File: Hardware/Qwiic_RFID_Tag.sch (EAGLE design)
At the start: 29 parts, among them J1 Qwiic, J2 Qwiic, U1 ST25DV64KC

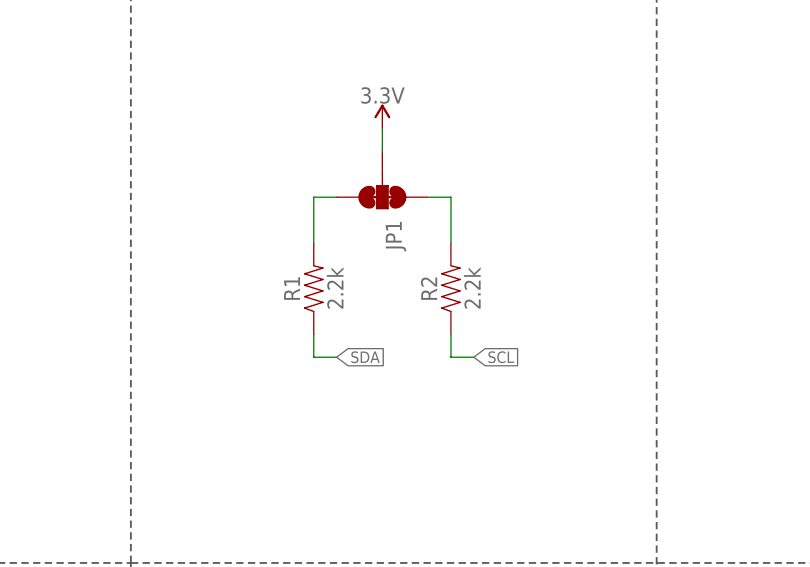
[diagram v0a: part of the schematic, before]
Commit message: Fixed misaligned mounting hole; trimmed long schematic segment.
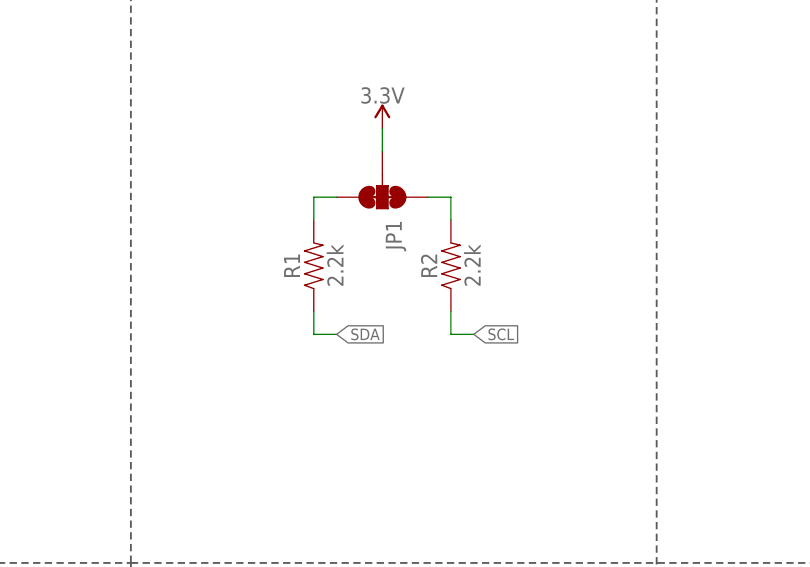
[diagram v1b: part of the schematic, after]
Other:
- moved on the sheet: R1, R2
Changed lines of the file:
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@@
 <attribute name="VALUE" x="174.625" y="122.428" size="1.778" layer="96" font="vector" rot="R90" align="top-left"/>
 </instance>
-<instance part="R1" gate="G$1" x="109.22" y="134.62" smashed="yes" rot="R90">
-<attribute name="NAME" x="107.696" y="134.62" size="1.778" layer="95" font="vector" rot="R90" align="bottom-center"/>
-<attribute name="VALUE" x="110.744" y="134.62" size="1.778" layer="96" font="vector" rot="R90" align="top-center"/>
-</instance>
-<instance part="R2" gate="G$1" x="124.46" y="134.62" smashed="yes" rot="R90">
-<attribute name="NAME" x="122.936" y="134.62" size="1.778" layer="95" font="vector" rot="R90" align="bottom-center"/>
-<attribute name="VALUE" x="125.984" y="134.62" size="1.778" layer="96" font="vector" rot="R90" align="top-center"/>
+<instance part="R1" gate="G$1" x="109.22" y="137.16" smashed="yes" rot="R90">
+<attribute name="NAME" x="107.696" y="137.16" size="1.778" layer="95" font="vector" rot="R90" align="bottom-center"/>
+<attribute name="VALUE" x="110.744" y="137.16" size="1.778" layer="96" font="vector" rot="R90" align="top-center"/>
+</instance>
+<instance part="R2" gate="G$1" x="124.46" y="137.16" smashed="yes" rot="R90">
+<attribute name="NAME" x="122.936" y="137.16" size="1.778" layer="95" font="vector" rot="R90" align="bottom-center"/>
+<attribute name="VALUE" x="125.984" y="137.16" size="1.778" layer="96" font="vector" rot="R90" align="top-center"/>
 </instance>
 <instance part="JP1" gate="G$1" x="116.84" y="144.78" smashed="yes" rot="R270">
@@
 <segment>
 <pinref part="R2" gate="G$1" pin="1"/>
-<wire x1="124.46" y1="129.54" x2="124.46" y2="127" width="0.1524" layer="91"/>
-<wire x1="124.46" y1="127" x2="127" y2="127" width="0.1524" layer="91"/>
-<label x="127" y="127" size="1.27" layer="95" xref="yes"/>
+<wire x1="124.46" y1="132.08" x2="124.46" y2="129.54" width="0.1524" layer="91"/>
+<wire x1="124.46" y1="129.54" x2="127" y2="129.54" width="0.1524" layer="91"/>
+<label x="127" y="129.54" size="1.27" layer="95" xref="yes"/>
 </segment>
 <segment>
@@
 <segment>
 <pinref part="R1" gate="G$1" pin="1"/>
-<wire x1="109.22" y1="129.54" x2="109.22" y2="127" width="0.1524" layer="91"/>
-<wire x1="109.22" y1="127" x2="111.76" y2="127" width="0.1524" layer="91"/>
-<label x="111.76" y="127" size="1.27" layer="95" xref="yes"/>
+<wire x1="109.22" y1="132.08" x2="109.22" y2="129.54" width="0.1524" layer="91"/>
+<wire x1="109.22" y1="129.54" x2="111.76" y2="129.54" width="0.1524" layer="91"/>
+<label x="111.76" y="129.54" size="1.27" layer="95" xref="yes"/>
 </segment>
 <segment>
@@
 <segment>
 <pinref part="R1" gate="G$1" pin="2"/>
-<wire x1="109.22" y1="139.7" x2="109.22" y2="144.78" width="0.1524" layer="91"/>
+<wire x1="109.22" y1="142.24" x2="109.22" y2="144.78" width="0.1524" layer="91"/>
 <wire x1="109.22" y1="144.78" x2="111.76" y2="144.78" width="0.1524" layer="91"/>
 <pinref part="JP1" gate="G$1" pin="3"/>
@@
 <pinref part="R2" gate="G$1" pin="2"/>
 <wire x1="121.92" y1="144.78" x2="124.46" y2="144.78" width="0.1524" layer="91"/>
-<wire x1="124.46" y1="144.78" x2="124.46" y2="139.7" width="0.1524" layer="91"/>
+<wire x1="124.46" y1="144.78" x2="124.46" y2="142.24" width="0.1524" layer="91"/>
 <pinref part="JP1" gate="G$1" pin="1"/>
 </segment>

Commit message: Created PCB production files.
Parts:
- LOGO2, LOGO3: value QWIIC_LOGO_4MM -> QWIIC_LOGO_7MM; device SparkFun-Aesthetics:QWIIC_LOGO_4MM -> SparkFun-Aesthetics:QWIIC_LOGO_7MM
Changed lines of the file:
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@@
 <part name="FD4" library="SparkFun-Aesthetics" deviceset="FIDUCIAL" device="1X2"/>
 <part name="LOGO1" library="SparkFun-Aesthetics" deviceset="OSHW-LOGO" device="MINI" value="OSHW-LOGOMINI"/>
-<part name="LOGO2" library="SparkFun-Aesthetics" deviceset="QWIIC_LOGO" device="_4MM" value="QWIIC_LOGO_4MM"/>
-<part name="LOGO3" library="SparkFun-Aesthetics" deviceset="QWIIC_LOGO" device="_4MM" value="QWIIC_LOGO_4MM"/>
+<part name="LOGO3" library="SparkFun-Aesthetics" deviceset="QWIIC_LOGO" device="_7MM" value="QWIIC_LOGO_7MM"/>
 <part name="H1" library="SparkFun-Hardware" deviceset="STAND-OFF" device=""/>
 <part name="H2" library="SparkFun-Hardware" deviceset="STAND-OFF" device=""/>
@@
 <part name="U$1" library="SparkX" deviceset="SPARKX-LOGO" device="5"/>
 <part name="U$2" library="SparkX" deviceset="SPARKX-LOGO" device="5"/>
+<part name="LOGO2" library="SparkFun-Aesthetics" deviceset="QWIIC_LOGO" device="_7MM" value="QWIIC_LOGO_7MM"/>
 </parts>
 <sheets>
@@
 <instance part="FD4" gate="G$1" x="233.68" y="30.48" smashed="yes"/>
 <instance part="LOGO1" gate="G$1" x="83.82" y="25.4" smashed="yes"/>
-<instance part="LOGO2" gate="G$1" x="116.84" y="17.78" smashed="yes"/>
-<instance part="LOGO3" gate="G$1" x="116.84" y="17.78" smashed="yes"/>
+<instance part="LOGO3" gate="G$1" x="116.84" y="20.32" smashed="yes"/>
 <instance part="H1" gate="G$1" x="238.76" y="27.94" smashed="yes"/>
 <instance part="H2" gate="G$1" x="241.3" y="27.94" smashed="yes"/>
@@
 <instance part="U$1" gate="G$1" x="116.84" y="27.94" smashed="yes"/>
 <instance part="U$2" gate="G$1" x="116.84" y="27.94" smashed="yes"/>
+<instance part="LOGO2" gate="G$1" x="116.84" y="20.32" smashed="yes"/>
 </instances>
 <busses>

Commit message: X02 PCB
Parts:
- removed LOGO2: QWIIC_LOGO_7MM, SparkFun-Aesthetics:QWIIC_LOGO_7MM
- FRAME1: REV (none) -> X02; VERSION (none) -> x01
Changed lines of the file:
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@@
 <setting verticaltext="up"/>
 </settings>
-<grid distance="0.1" unitdist="inch" unit="inch" style="lines" multiple="1" display="no" altdistance="0.01" altunitdist="inch" altunit="inch"/>
+<grid distance="0.1" unitdist="inch" unit="inch" style="lines" multiple="1" display="no" altdistance="0.05" altunitdist="inch" altunit="inch"/>
 <layers>
 <layer number="1" name="Top" color="4" fill="1" visible="no" active="no"/>
 <layer number="2" name="Route2" color="1" fill="3" visible="no" active="no"/>
+<layer number="3" name="Route3" color="4" fill="3" visible="no" active="no"/>
+<layer number="4" name="Route4" color="1" fill="4" visible="no" active="no"/>
+<layer number="5" name="Route5" color="4" fill="4" visible="no" active="no"/>
+<layer number="6" name="Route6" color="1" fill="8" visible="no" active="no"/>
+<layer number="7" name="Route7" color="4" fill="8" visible="no" active="no"/>
+<layer number="8" name="Route8" color="1" fill="2" visible="no" active="no"/>
+<layer number="9" name="Route9" color="4" fill="2" visible="no" active="no"/>
+<layer number="10" name="Route10" color="1" fill="7" visible="no" active="no"/>
+<layer number="11" name="Route11" color="4" fill="7" visible="no" active="no"/>
+<layer number="12" name="Route12" color="1" fill="5" visible="no" active="no"/>
+<layer number="13" name="Route13" color="4" fill="5" visible="no" active="no"/>
+<layer number="14" name="Route14" color="1" fill="6" visible="no" active="no"/>
 <layer number="15" name="Route15" color="4" fill="6" visible="no" active="no"/>
 <layer number="16" name="Bottom" color="1" fill="1" visible="no" active="no"/>
@@
 <part name="FRAME1" library="SparkFun-Aesthetics" deviceset="FRAME-LETTER" device="NO_PACKAGE">
 <attribute name="DESIGNER" value="Ricardo Ramos"/>
+<attribute name="REV" value="X02"/>
+<attribute name="VERSION" value="x01"/>
 </part>
 <part name="L1" library="SparkFun-Coils" deviceset="PCB_4UH_INDUCTOR" device=""/>
@@
 <part name="U$1" library="SparkX" deviceset="SPARKX-LOGO" device="5"/>
 <part name="U$2" library="SparkX" deviceset="SPARKX-LOGO" device="5"/>
-<part name="LOGO2" library="SparkFun-Aesthetics" deviceset="QWIIC_LOGO" device="_7MM" value="QWIIC_LOGO_7MM"/>
 </parts>
 <sheets>
 <sheet>
 <plain>
-<text x="200.66" y="93.98" size="2.54" layer="94" align="center">Qwiic Connectors</text>
-<text x="162.56" y="168.91" size="1.27" layer="97">Cut trace to disable LED</text>
-<text x="210.82" y="168.91" size="1.27" layer="97">Cut trace to remove !GPO! pullup</text>
-<text x="119.38" y="93.98" size="2.54" layer="94" align="center">0.1" Header</text>
-<text x="45.72" y="93.98" size="2.54" layer="94" align="center">PCB antenna</text>
-<text x="116.84" y="172.72" size="2.54" layer="94" align="center">I2C Pullup</text>
-<text x="172.72" y="172.72" size="2.54" layer="94" align="center">Power LED</text>
-<text x="223.52" y="172.72" size="2.54" layer="94" align="center">!GPO! Pullup</text>
-<text x="45.72" y="170.18" size="2.54" layer="94" align="center">ST25DV64KC Dynamic RFID Tag</text>
-<text x="27.94" y="40.64" size="2.54" layer="94" align="center">Power decoupling</text>
+<text x="200.66" y="93.98" size="2.54" layer="94" font="vector" align="center">Qwiic Connectors</text>
+<text x="162.56" y="168.91" size="1.27" layer="97" font="vector">Cut trace to disable LED</text>
+<text x="210.82" y="168.91" size="1.27" layer="97" font="vector">Cut trace to remove !GPO! pullup</text>
+<text x="119.38" y="93.98" size="2.54" layer="94" font="vector" align="center">0.1" Header</text>
+<text x="45.72" y="93.98" size="2.54" layer="94" font="vector" align="center">PCB antenna</text>
+<text x="116.84" y="172.72" size="2.54" layer="94" font="vector" align="center">I2C Pullup</text>
+<text x="172.72" y="172.72" size="2.54" layer="94" font="vector" align="center">Power LED</text>
+<text x="223.52" y="172.72" size="2.54" layer="94" font="vector" align="center">!GPO! Pullup</text>
+<text x="45.72" y="170.18" size="2.54" layer="94" font="vector" align="center">ST25DV64KC Dynamic RFID Tag</text>
+<text x="27.94" y="40.64" size="2.54" layer="94" font="vector" align="center">Power decoupling</text>
 <wire x1="0" y1="104.14" x2="88.9" y2="104.14" width="0.2032" layer="97" style="longdash"/>
 <wire x1="88.9" y1="104.14" x2="198.12" y2="104.14" width="0.2032" layer="97" style="longdash"/>
@@
 <wire x1="147.32" y1="185.42" x2="147.32" y2="50.8" width="0.2032" layer="97" style="longdash"/>
 <wire x1="198.12" y1="104.14" x2="198.12" y2="185.42" width="0.2032" layer="97" style="longdash"/>
-<text x="104.14" y="168.91" size="1.27" layer="97">Cut trace to disable I2C pullups</text>
-<text x="45.72" y="59.69" size="1.27" layer="97" align="center">C2 may be changed to improve circuit resonance.
+<text x="104.14" y="168.91" size="1.27" layer="97" font="vector">Cut trace to disable I2C pullups</text>
+<text x="45.72" y="59.69" size="1.27" layer="97" font="vector" align="center">C2 may be changed to improve circuit resonance.
 5.6 pF is the initial calculated value.</text>
 <wire x1="58.42" y1="50.8" x2="58.42" y2="0" width="0.2032" layer="97" style="longdash"/>
@@
 <attribute name="NAME" x="205.74" y="71.374" size="1.778" layer="95" font="vector"/>
 </instance>
-<instance part="FRAME1" gate="G$1" x="0" y="0" smashed="yes"/>
+<instance part="FRAME1" gate="G$1" x="0" y="0" smashed="yes">
+<attribute name="REV" x="238.76" y="7.62" size="1.778" layer="94" font="vector"/>
+</instance>
 <instance part="FRAME1" gate="V" x="147.32" y="0" smashed="yes">
 <attribute name="LAST_DATE_TIME" x="160.02" y="1.27" size="2.54" layer="94" font="vector"/>
@@
 <attribute name="VALUE" x="29.464" y="18.161" size="1.778" layer="96" font="vector"/>
 </instance>
-<instance part="J3" gate="G$1" x="111.76" y="71.12" smashed="yes">
+<instance part="J3" gate="JP1" x="111.76" y="71.12" smashed="yes">
 <attribute name="VALUE" x="106.68" y="61.214" size="1.778" layer="96" font="vector"/>
 <attribute name="NAME" x="106.68" y="81.788" size="1.778" layer="95" font="vector"/>
@@
 <instance part="U$1" gate="G$1" x="116.84" y="27.94" smashed="yes"/>
 <instance part="U$2" gate="G$1" x="116.84" y="27.94" smashed="yes"/>
-<instance part="LOGO2" gate="G$1" x="116.84" y="20.32" smashed="yes"/>
 </instances>
 <busses>
@@
 <pinref part="GND6" gate="1" pin="GND"/>
 <wire x1="119.38" y1="66.04" x2="119.38" y2="63.5" width="0.1524" layer="91"/>
-<pinref part="J3" gate="G$1" pin="1"/>
+<pinref part="J3" gate="JP1" pin="1"/>
 <wire x1="116.84" y1="66.04" x2="119.38" y2="66.04" width="0.1524" layer="91"/>
 </segment>
@@
 <segment>
 <pinref part="SUPPLY8" gate="G$1" pin="3.3V"/>
-<pinref part="J3" gate="G$1" pin="2"/>
+<pinref part="J3" gate="JP1" pin="2"/>
 <wire x1="116.84" y1="68.58" x2="119.38" y2="68.58" width="0.1524" layer="91"/>
 <wire x1="119.38" y1="68.58" x2="119.38" y2="81.28" width="0.1524" layer="91"/>
@@
 </segment>
 <segment>
-<pinref part="J3" gate="G$1" pin="4"/>
+<pinref part="J3" gate="JP1" pin="4"/>
 <wire x1="116.84" y1="73.66" x2="121.92" y2="73.66" width="0.1524" layer="91"/>
 <label x="121.92" y="73.66" size="1.27" layer="95" xref="yes"/>
@@
 </segment>
 <segment>
-<pinref part="J3" gate="G$1" pin="3"/>
+<pinref part="J3" gate="JP1" pin="3"/>
 <wire x1="116.84" y1="71.12" x2="121.92" y2="71.12" width="0.1524" layer="91"/>
 <label x="121.92" y="71.12" size="1.27" layer="95" xref="yes"/>
@@
 </segment>
 <segment>
-<pinref part="J3" gate="G$1" pin="6"/>
+<pinref part="J3" gate="JP1" pin="6"/>
 <wire x1="116.84" y1="78.74" x2="121.92" y2="78.74" width="0.1524" layer="91"/>
 <label x="121.92" y="78.74" size="1.27" layer="95" xref="yes"/>
@@
 </segment>
 <segment>
-<pinref part="J3" gate="G$1" pin="5"/>
+<pinref part="J3" gate="JP1" pin="5"/>
 <wire x1="116.84" y1="76.2" x2="121.92" y2="76.2" width="0.1524" layer="91"/>
 <label x="121.92" y="76.2" size="1.27" layer="95" xref="yes"/>
@@
 </sheet>
 </sheets>
+<errors>
+</errors>
 </schematic>
 </drawing>
